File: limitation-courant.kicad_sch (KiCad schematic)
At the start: 24 parts, among them U14 TSV791, U15 ATL431, U16 LMV7219, U17 SN74LVC1G132, U18 SN74LVC1G74, U19 ISO7710F

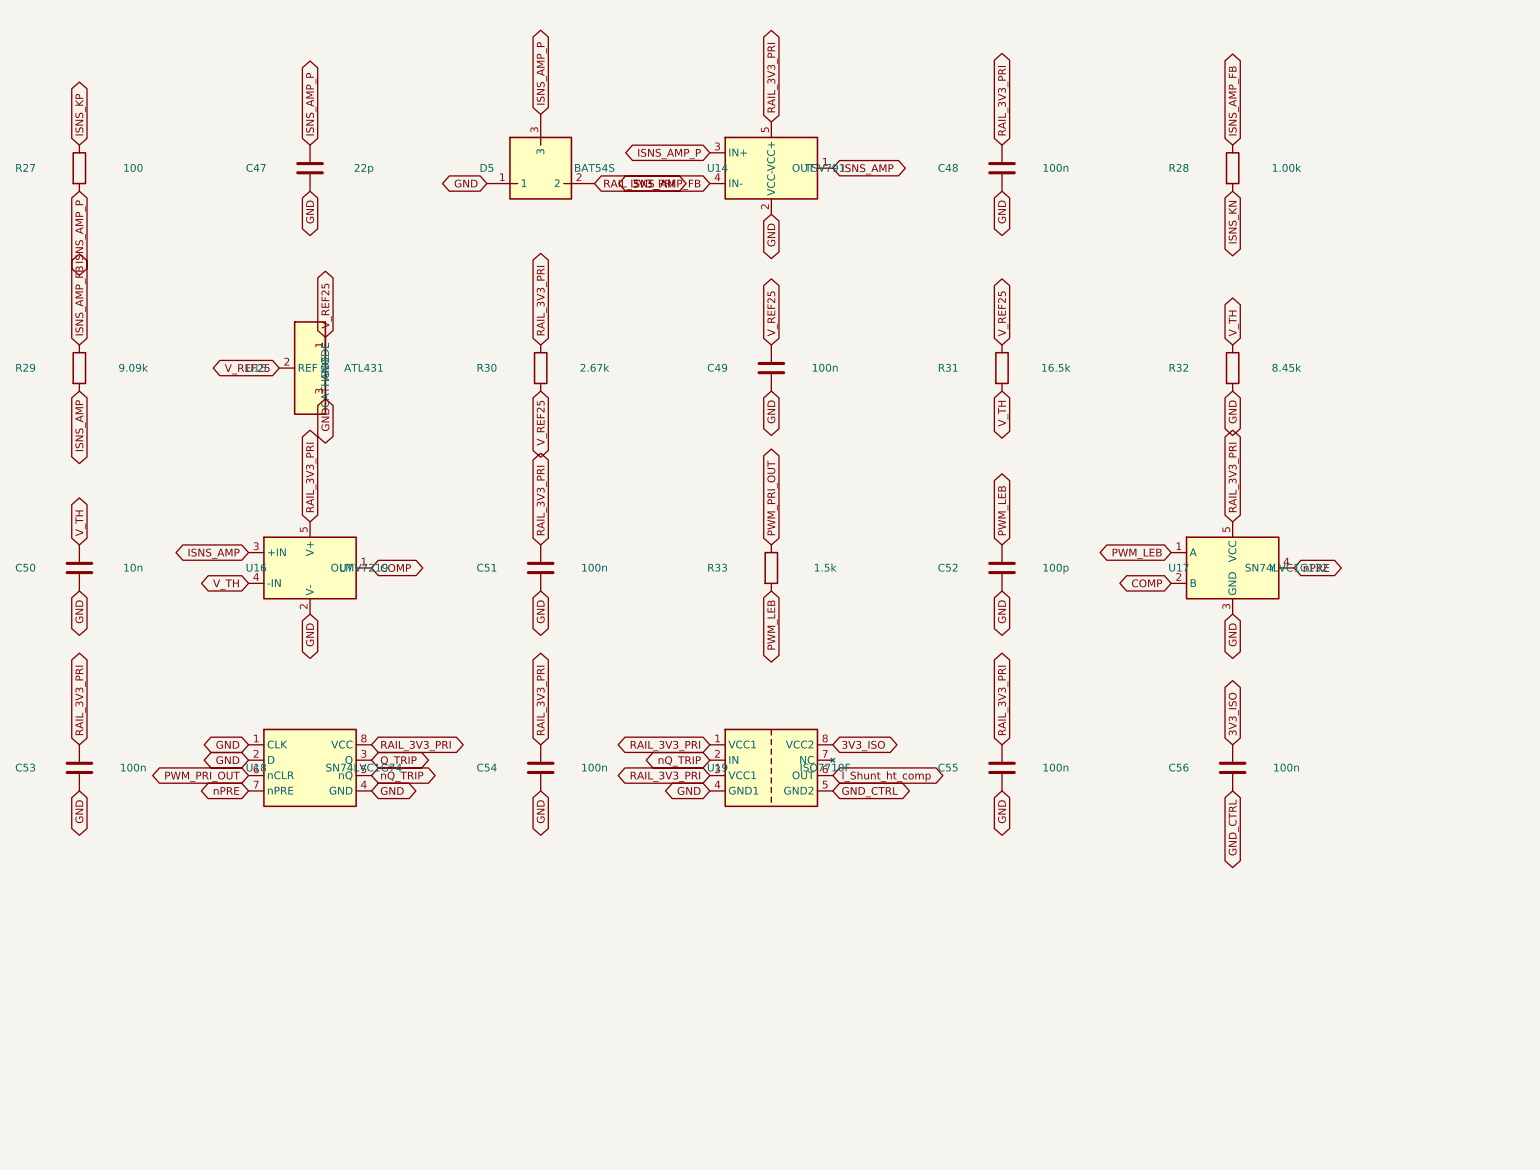
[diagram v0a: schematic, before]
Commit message: Ajoute une LED de defaut sur Q_TRIP (R34/D6), corrige un bug d'insertion lib_symbols
Q_TRIP (sortie de reserve du verrou) recoit un usage reel : LED rouge 3mm
+ 10k, polarite ajustee par l'utilisateur pour s'allumer en defaut latche
(Q_TRIP -> D6 -> R34 -> GND, verifie par export netlist).

Corrige au passage une insertion incorrecte du bloc lib_symbols de
Device:LED (imbrique par erreur dans l'etiquette globale ISNS_AMP au lieu
de suivre la vraie fermeture de lib_symbols), qui empechait le chargement
de la feuille. Documente dans l'addendum du S19.

Co-Authored-By: Claude Sonnet 5 <noreply@anthropic.com>
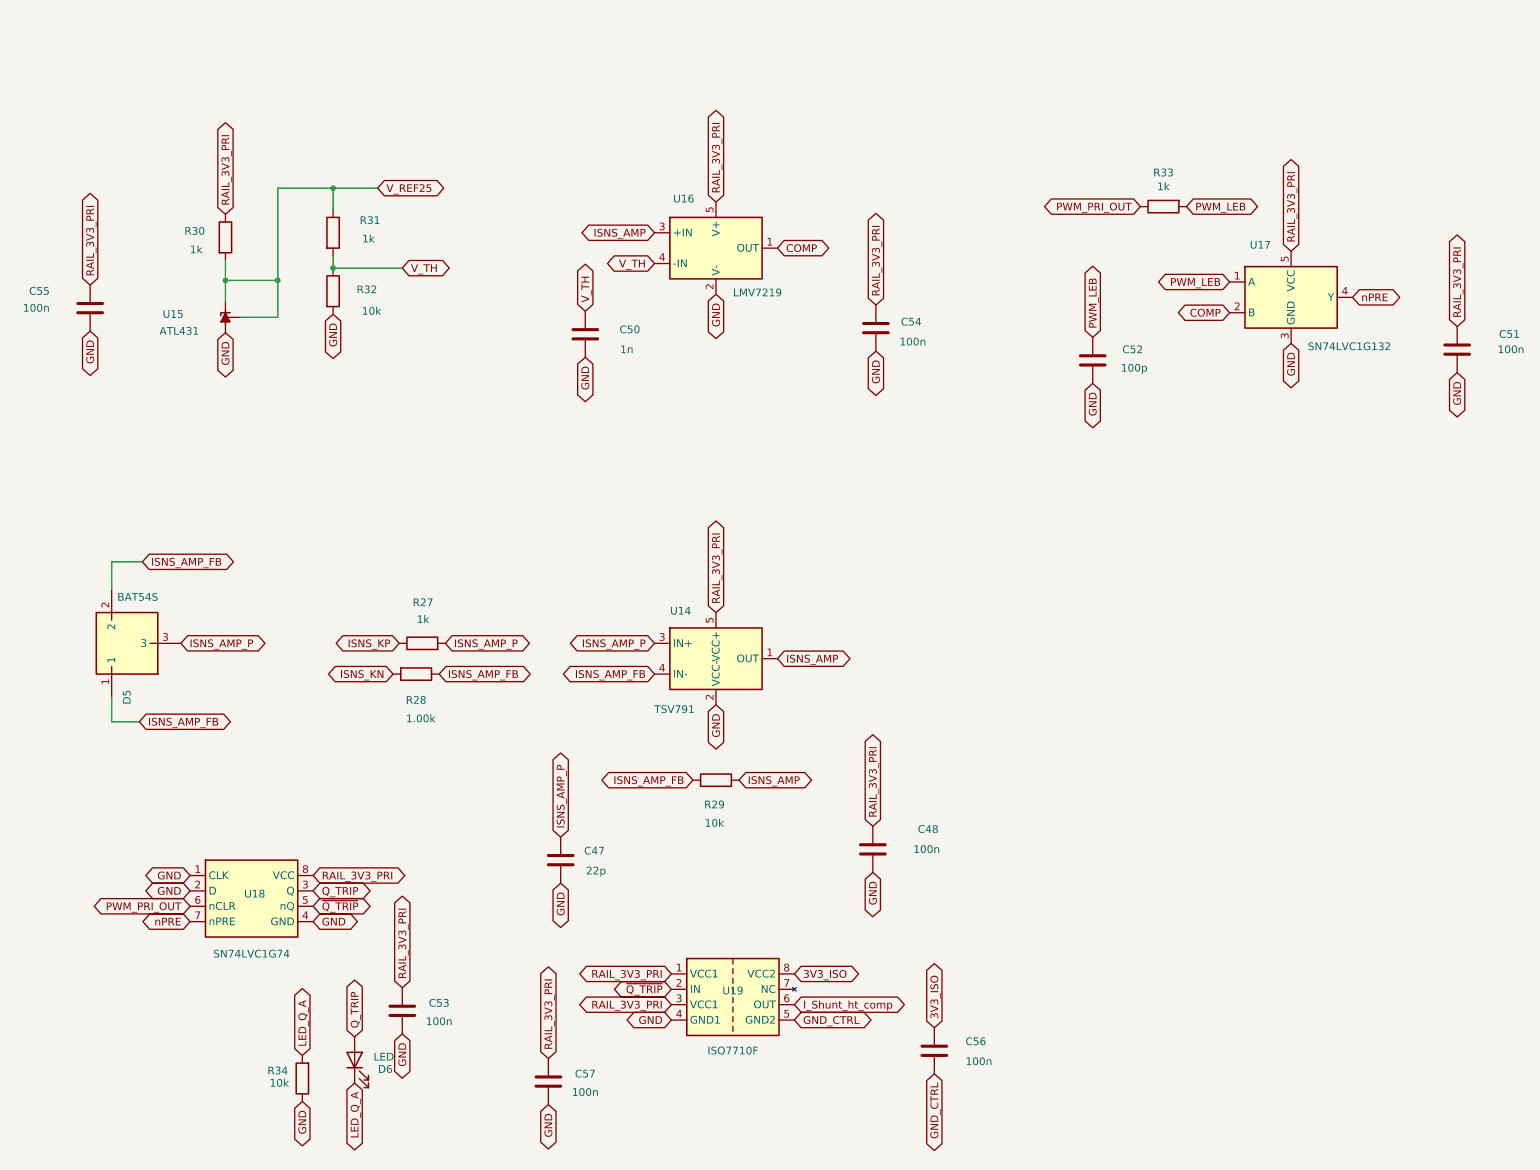
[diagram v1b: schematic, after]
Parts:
- removed C49: 100n, Capacitor_SMD:C_0805_2012Metric, symbol Device:C
- added C57: 100n, Capacitor_SMD:C_0805_2012Metric, symbol Device:C
- added D6: LED, LED_THT:LED_D3.0mm, symbol Device:LED
- added R34: 10k, Resistor_SMD:R_0805_2012Metric, symbol Device:R
- C50: value 10n -> 1n
- R27: value 100 -> 1k
- R29: value 9.09k -> 10k
- R30: value 2.67k -> 1k
- R31: value 16.5k -> 1k
- R32: value 8.45k -> 10k
- R33: value 1.5k -> 1k
- U15: symbol custom_parts:ATL431 -> Reference_Voltage:TL431DBZ
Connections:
- net GND: now also C57.2, R34.1; no longer D5.1
- net ISNS_AMP_FB: now also D5.1, D5.2
- net Q_TRIP: now also D6.2 (A)
- net RAIL_3V3_PRI: now also C57.1; no longer D5.2
- net nQ_TRIP renamed ~{Q_TRIP}
- new net LED_Q_A: D6.1 (K), R34.2
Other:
- moved on the sheet: C47, C48, C50, C51, C52, C53, C54, C55, C56, D5, R27, R28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

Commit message: Retouches manuelles : notation ~{} pour nPRE/nQ_TRIP, RAIL_8V25->RAIL_3V3_PRI, via 1.0/0.4mm
Renomme nPRE et nQ_TRIP en notation KiCad overline (~{PRE}/~{Q_TRIP}),
corrige une etiquette RAIL_8V25 en RAIL_3V3_PRI dans isolation.kicad_sch,
ajuste la taille de via par defaut (1.8/0.8 -> 1.0/0.4mm) et progresse sur
le placement/routage PCB.

Co-Authored-By: Claude Sonnet 5 <noreply@anthropic.com>
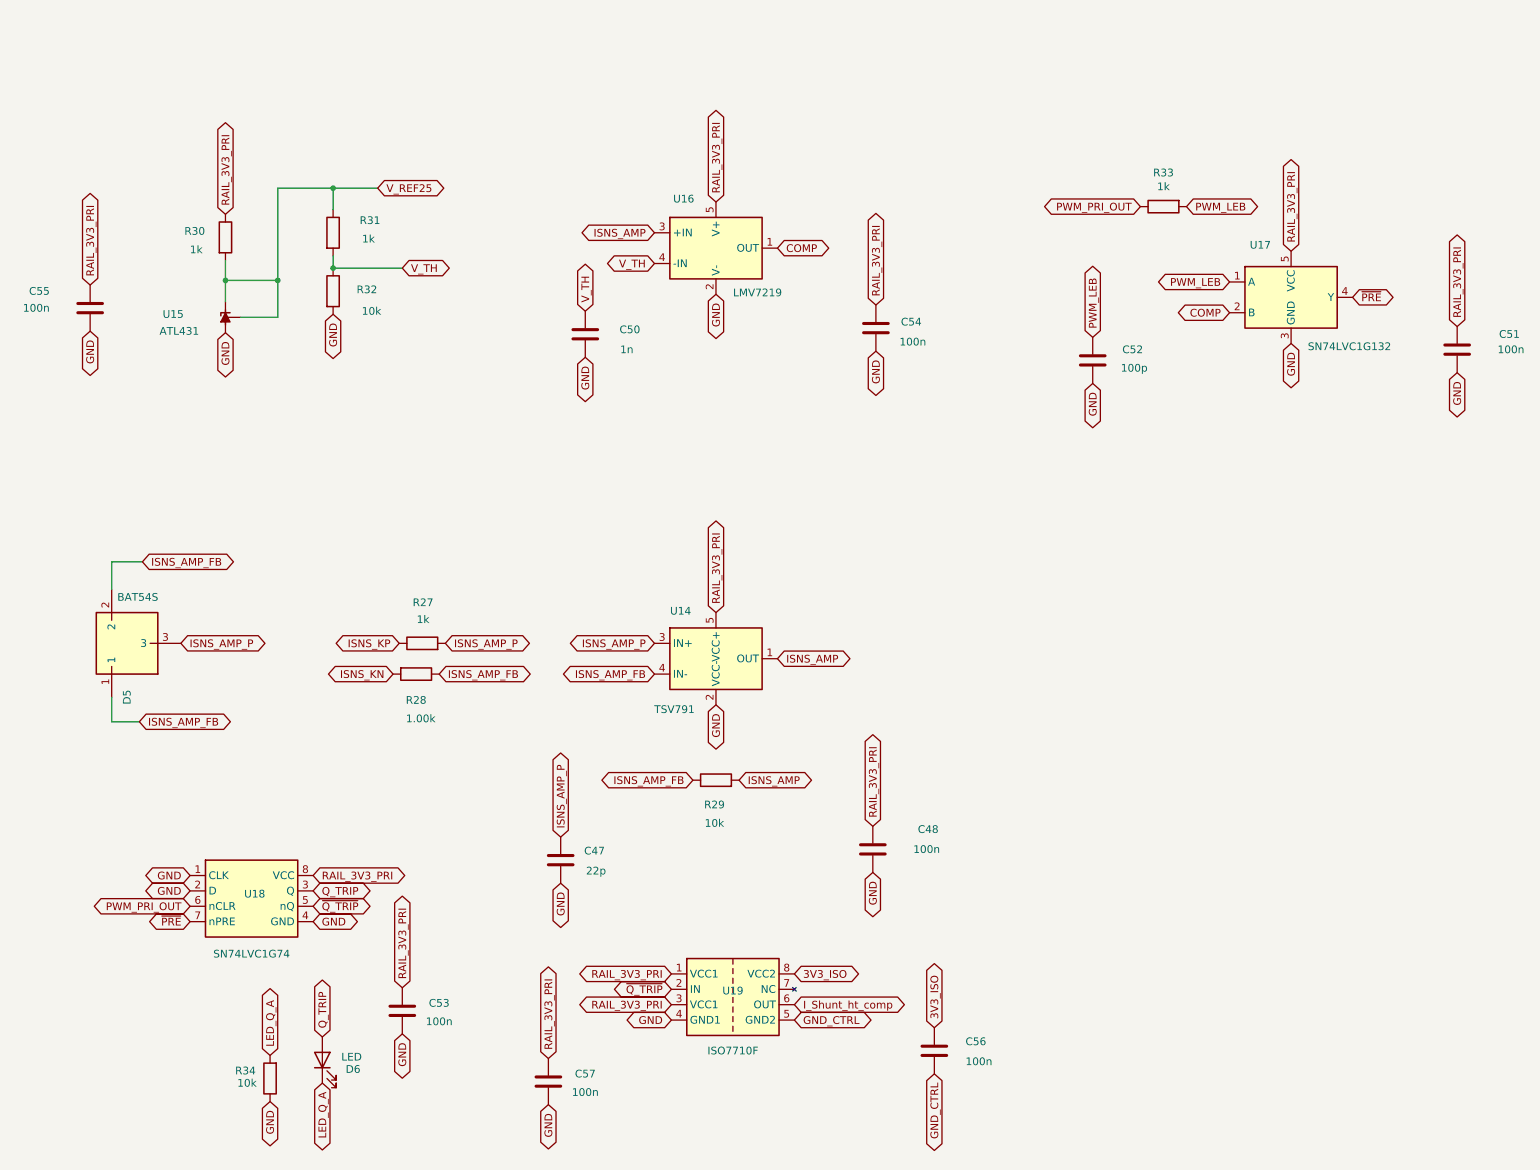
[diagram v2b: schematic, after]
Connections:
- net nPRE renamed ~{PRE}
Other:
- moved on the sheet: D6, R34
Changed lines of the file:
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@@
 	(global_label "LED_Q_A"
 		(shape bidirectional)
-		(at 70.866 176.53 270)
-		(fields_autoplaced yes)
-		(effects
-			(font
-				(size 1.27 1.27)
-			)
-			(justify right)
-		)
-		(property "Intersheetrefs" "${INTERSHEET_REFS}"
-			(at 70.866 188.4279 90)
+		(at 65.532 176.53 270)
+		(fields_autoplaced yes)
+		(effects
+			(font
+				(size 1.27 1.27)
+			)
+			(justify right)
+		)
+		(property "Intersheetrefs" "${INTERSHEET_REFS}"
+			(at 65.532 188.4279 90)
 			(hide yes)
 			(show_name no)
@@
 	(global_label "LED_Q_A"
 		(shape bidirectional)
-		(at 62.23 171.958 90)
-		(fields_autoplaced yes)
-		(effects
-			(font
-				(size 1.27 1.27)
-			)
-			(justify left)
-		)
-		(property "Intersheetrefs" "${INTERSHEET_REFS}"
-			(at 62.23 160.0601 90)
+		(at 56.896 171.958 90)
+		(fields_autoplaced yes)
+		(effects
+			(font
+				(size 1.27 1.27)
+			)
+			(justify left)
+		)
+		(property "Intersheetrefs" "${INTERSHEET_REFS}"
+			(at 56.896 160.0601 90)
 			(hide yes)
 			(show_name no)
@@
 	(global_label "GND"
 		(shape bidirectional)
-		(at 62.23 179.578 270)
-		(fields_autoplaced yes)
-		(effects
-			(font
-				(size 1.27 1.27)
-			)
-			(justify right)
-		)
-		(property "Intersheetrefs" "${INTERSHEET_REFS}"
-			(at 62.23 187.545 90)
+		(at 56.896 179.578 270)
+		(fields_autoplaced yes)
+		(effects
+			(font
+				(size 1.27 1.27)
+			)
+			(justify right)
+		)
+		(property "Intersheetrefs" "${INTERSHEET_REFS}"
+			(at 56.896 187.545 90)
 			(hide yes)
 			(show_name no)
@@
 		)
 	)
-	(global_label "nPRE"
+	(global_label "~{PRE}"
 		(shape bidirectional)
 		(at 235.712 46.736 0)
@@
 		)
 		(property "Intersheetrefs" "${INTERSHEET_REFS}"
-			(at 235.712 46.736 0)
-			(hide yes)
-			(show_name no)
-			(do_not_autoplace no)
-			(effects
-				(font
-					(size 1.27 1.27)
-				)
-			)
-		)
-	)
-	(global_label "nPRE"
+			(at 243.4975 46.736 0)
+			(hide yes)
+			(show_name no)
+			(do_not_autoplace no)
+			(effects
+				(font
+					(size 1.27 1.27)
+				)
+				(justify left)
+			)
+		)
+	)
+	(global_label "~{PRE}"
 		(shape bidirectional)
 		(at 43.688 149.86 180)
@@
 		)
 		(property "Intersheetrefs" "${INTERSHEET_REFS}"
-			(at 43.688 149.86 0)
-			(hide yes)
-			(show_name no)
-			(do_not_autoplace no)
-			(effects
-				(font
-					(size 1.27 1.27)
-				)
+			(at 35.9025 149.86 0)
+			(hide yes)
+			(show_name no)
+			(do_not_autoplace no)
+			(effects
+				(font
+					(size 1.27 1.27)
+				)
+				(justify right)
 			)
 		)
@@
 	(global_label "Q_TRIP"
 		(shape bidirectional)
-		(at 70.866 168.91 90)
-		(fields_autoplaced yes)
-		(effects
-			(font
-				(size 1.27 1.27)
-			)
-			(justify left)
-		)
-		(property "Intersheetrefs" "${INTERSHEET_REFS}"
-			(at 70.866 158.403 90)
+		(at 65.532 168.91 90)
+		(fields_autoplaced yes)
+		(effects
+			(font
+				(size 1.27 1.27)
+			)
+			(justify left)
+		)
+		(property "Intersheetrefs" "${INTERSHEET_REFS}"
+			(at 65.532 158.403 90)
 			(hide yes)
 			(show_name no)
@@
 	(symbol
 		(lib_id "Device:R")
-		(at 62.23 175.768 180)
+		(at 56.896 175.768 180)
 		(unit 1)
 		(body_style 1)
@@
 		(dnp no)
 		(property "Reference" "R34"
-			(at 58.166 174.498 0)
+			(at 52.832 174.498 0)
 			(show_name no)
 			(do_not_autoplace no)
@@
 		)
 		(property "Value" "10k"
-			(at 58.42 176.53 0)
+			(at 53.086 176.53 0)
 			(show_name no)
 			(do_not_autoplace no)
@@
 		)
 		(property "Footprint" "Resistor_SMD:R_0805_2012Metric"
-			(at 62.23 175.768 0)
+			(at 56.896 175.768 0)
 			(hide yes)
 			(show_name no)
@@
 		)
 		(property "Datasheet" ""
-			(at 62.23 175.768 0)
+			(at 56.896 175.768 0)
 			(hide yes)
 			(show_name no)
@@
 		)
 		(property "Description" "LED de defaut Q_TRIP (D6) -- resistance de limitation de courant"
-			(at 62.23 175.768 0)
+			(at 56.896 175.768 0)
 			(hide yes)
 			(show_name no)
@@
 	(symbol
 		(lib_id "Device:LED")
-		(at 70.866 172.72 90)
+		(at 65.532 172.72 90)
 		(unit 1)
 		(body_style 1)
@@
 		(dnp no)
 		(property "Reference" "D6"
-			(at 75.946 174.244 90)
+			(at 70.612 174.244 90)
 			(show_name no)
 			(do_not_autoplace no)
@@
 		)
 		(property "Value" "LED"
-			(at 75.692 172.212 90)
+			(at 70.358 172.212 90)
 			(show_name no)
 			(do_not_autoplace no)
@@
 		)
 		(property "Footprint" "LED_THT:LED_D3.0mm"
-			(at 70.866 172.72 0)
+			(at 65.532 172.72 0)
 			(hide yes)
 			(show_name no)
@@
 		)
 		(property "Datasheet" ""
-			(at 70.866 172.72 0)
+			(at 65.532 172.72 0)
 			(hide yes)
 			(show_name no)
@@
 		)
 		(property "Description" "LED rouge 3mm, defaut latche (Q_TRIP)"
-			(at 70.866 172.72 0)
-			(hide yes)
-			(show_name no)
+			(at 65.532 172.72 0)
+			(hide yes)
+			(show_name no)

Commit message: Routage en cours : retouches schema (alim/flyback/isolation/limitation-courant/polarisation), doc renommage Temp_ht->I_Out_ht et NAPPE_FILAMENT_HT->DC_HT, fix .kicad_dru (commentaires #), nettoyage simulation/results
Co-Authored-By: Claude Sonnet 5 <noreply@anthropic.com>
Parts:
- D6: value LED -> CURRENT_LIMIT
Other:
- moved on the sheet: D6, R34
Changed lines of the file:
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@@
 	(global_label "LED_Q_A"
 		(shape bidirectional)
-		(at 65.532 176.53 270)
-		(fields_autoplaced yes)
-		(effects
-			(font
-				(size 1.27 1.27)
-			)
-			(justify right)
-		)
-		(property "Intersheetrefs" "${INTERSHEET_REFS}"
-			(at 65.532 188.4279 90)
+		(at 58.166 175.768 270)
+		(fields_autoplaced yes)
+		(effects
+			(font
+				(size 1.27 1.27)
+			)
+			(justify right)
+		)
+		(property "Intersheetrefs" "${INTERSHEET_REFS}"
+			(at 58.166 187.6659 90)
 			(hide yes)
 			(show_name no)
@@
 	(global_label "LED_Q_A"
 		(shape bidirectional)
-		(at 56.896 171.958 90)
-		(fields_autoplaced yes)
-		(effects
-			(font
-				(size 1.27 1.27)
-			)
-			(justify left)
-		)
-		(property "Intersheetrefs" "${INTERSHEET_REFS}"
-			(at 56.896 160.0601 90)
+		(at 49.53 171.196 90)
+		(fields_autoplaced yes)
+		(effects
+			(font
+				(size 1.27 1.27)
+			)
+			(justify left)
+		)
+		(property "Intersheetrefs" "${INTERSHEET_REFS}"
+			(at 49.53 159.2981 90)
 			(hide yes)
 			(show_name no)
@@
 	(global_label "GND"
 		(shape bidirectional)
-		(at 56.896 179.578 270)
-		(fields_autoplaced yes)
-		(effects
-			(font
-				(size 1.27 1.27)
-			)
-			(justify right)
-		)
-		(property "Intersheetrefs" "${INTERSHEET_REFS}"
-			(at 56.896 187.545 90)
+		(at 49.53 178.816 270)
+		(fields_autoplaced yes)
+		(effects
+			(font
+				(size 1.27 1.27)
+			)
+			(justify right)
+		)
+		(property "Intersheetrefs" "${INTERSHEET_REFS}"
+			(at 49.53 186.783 90)
 			(hide yes)
 			(show_name no)
@@
 	(global_label "Q_TRIP"
 		(shape bidirectional)
-		(at 65.532 168.91 90)
-		(fields_autoplaced yes)
-		(effects
-			(font
-				(size 1.27 1.27)
-			)
-			(justify left)
-		)
-		(property "Intersheetrefs" "${INTERSHEET_REFS}"
-			(at 65.532 158.403 90)
+		(at 58.166 168.148 90)
+		(fields_autoplaced yes)
+		(effects
+			(font
+				(size 1.27 1.27)
+			)
+			(justify left)
+		)
+		(property "Intersheetrefs" "${INTERSHEET_REFS}"
+			(at 58.166 157.641 90)
 			(hide yes)
 			(show_name no)
@@
 	(symbol
 		(lib_id "Device:R")
-		(at 56.896 175.768 180)
+		(at 49.53 175.006 180)
 		(unit 1)
 		(body_style 1)
@@
 		(dnp no)
 		(property "Reference" "R34"
-			(at 52.832 174.498 0)
+			(at 45.466 173.736 0)
 			(show_name no)
 			(do_not_autoplace no)
@@
 		)
 		(property "Value" "10k"
-			(at 53.086 176.53 0)
+			(at 45.72 175.768 0)
 			(show_name no)
 			(do_not_autoplace no)
@@
 		)
 		(property "Footprint" "Resistor_SMD:R_0805_2012Metric"
-			(at 56.896 175.768 0)
+			(at 49.53 175.006 0)
 			(hide yes)
 			(show_name no)
@@
 		)
 		(property "Datasheet" ""
-			(at 56.896 175.768 0)
+			(at 49.53 175.006 0)
 			(hide yes)
 			(show_name no)
@@
 		)
 		(property "Description" "LED de defaut Q_TRIP (D6) -- resistance de limitation de courant"
-			(at 56.896 175.768 0)
+			(at 49.53 175.006 0)
 			(hide yes)
 			(show_name no)
@@
 	(symbol
 		(lib_id "Device:LED")
-		(at 65.532 172.72 90)
+		(at 58.166 171.958 90)
 		(unit 1)
 		(body_style 1)
@@
 		(dnp no)
 		(property "Reference" "D6"
-			(at 70.612 174.244 90)
-			(show_name no)
-			(do_not_autoplace no)
-			(effects
-				(font
-					(size 1.27 1.27)
-				)
-			)
-		)
-		(property "Value" "LED"
-			(at 70.358 172.212 90)
+			(at 63.246 173.482 90)
+			(show_name no)
+			(do_not_autoplace no)
+			(effects
+				(font
+					(size 1.27 1.27)
+				)
+			)
+		)
+		(property "Value" "CURRENT_LIMIT"
+			(at 67.056 168.91 90)
 			(show_name no)
 			(do_not_autoplace no)
@@
 		)
 		(property "Footprint" "LED_THT:LED_D3.0mm"
-			(at 65.532 172.72 0)
+			(at 58.166 171.958 0)
 			(hide yes)
 			(show_name no)
@@
 		)
 		(property "Datasheet" ""
-			(at 65.532 172.72 0)
+			(at 58.166 171.958 0)
 			(hide yes)
 			(show_name no)
@@
 		)
 		(property "Description" "LED rouge 3mm, defaut latche (Q_TRIP)"
-			(at 65.532 172.72 0)
-			(hide yes)
-			(show_name no)
+			(at 58.166 171.958 0)
+			(hide yes)
+			(show_name no)
